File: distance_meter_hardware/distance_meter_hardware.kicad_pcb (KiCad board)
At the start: 2 copper layers, 95.5 x 55.5 mm, 6 parts, among them J1 PPPC071LFBN-RC, J2 PPPC071LFBN-RC, J3 PPPC141LFBN-RC, J4 PPPC141LFBN-RC, J5 PPPC071LFBN-RC, J6 PPPC071LFBN-RC

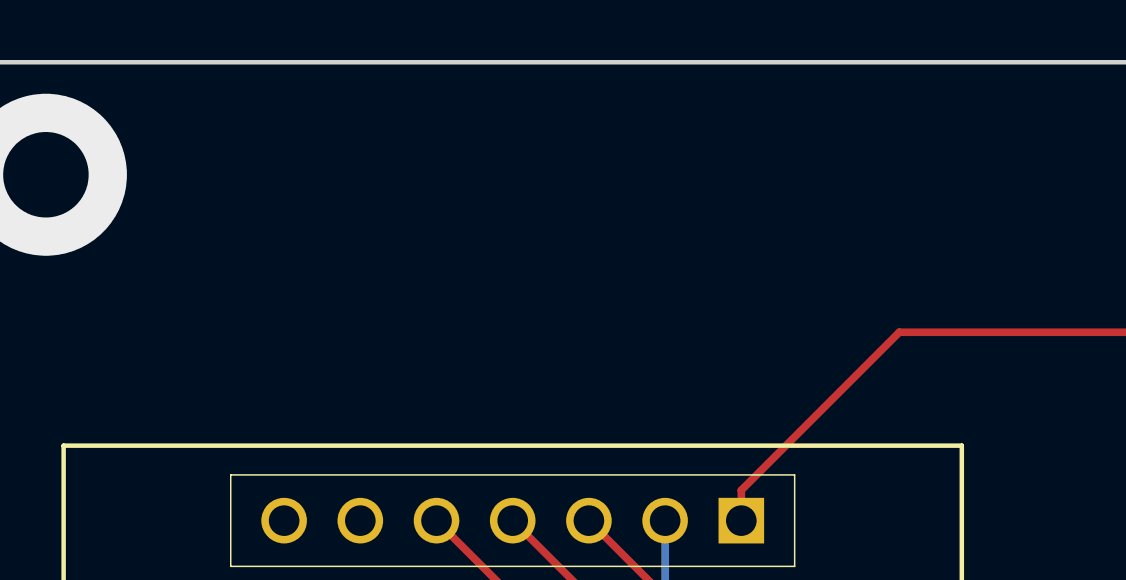
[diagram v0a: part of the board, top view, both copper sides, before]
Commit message: Add logo to PCB layout. Move measures to user-defined layer
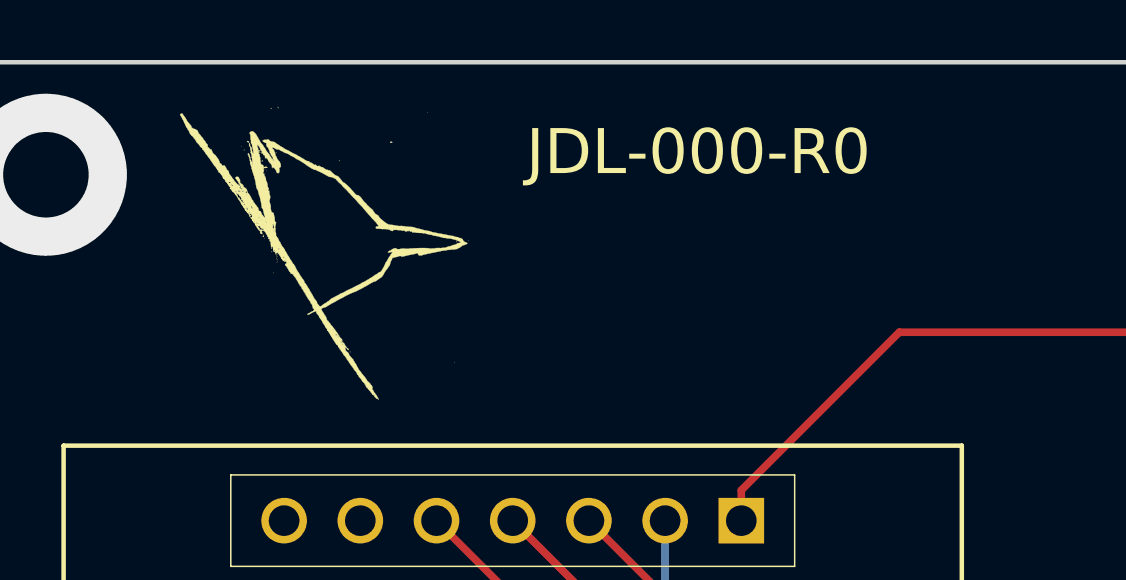
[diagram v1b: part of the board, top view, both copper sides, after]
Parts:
- added G***: LOGO, pictures:jaybird-logo-small, F.Cu at (71.4, 47.5)
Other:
- board text added: "JDL-000-R0"

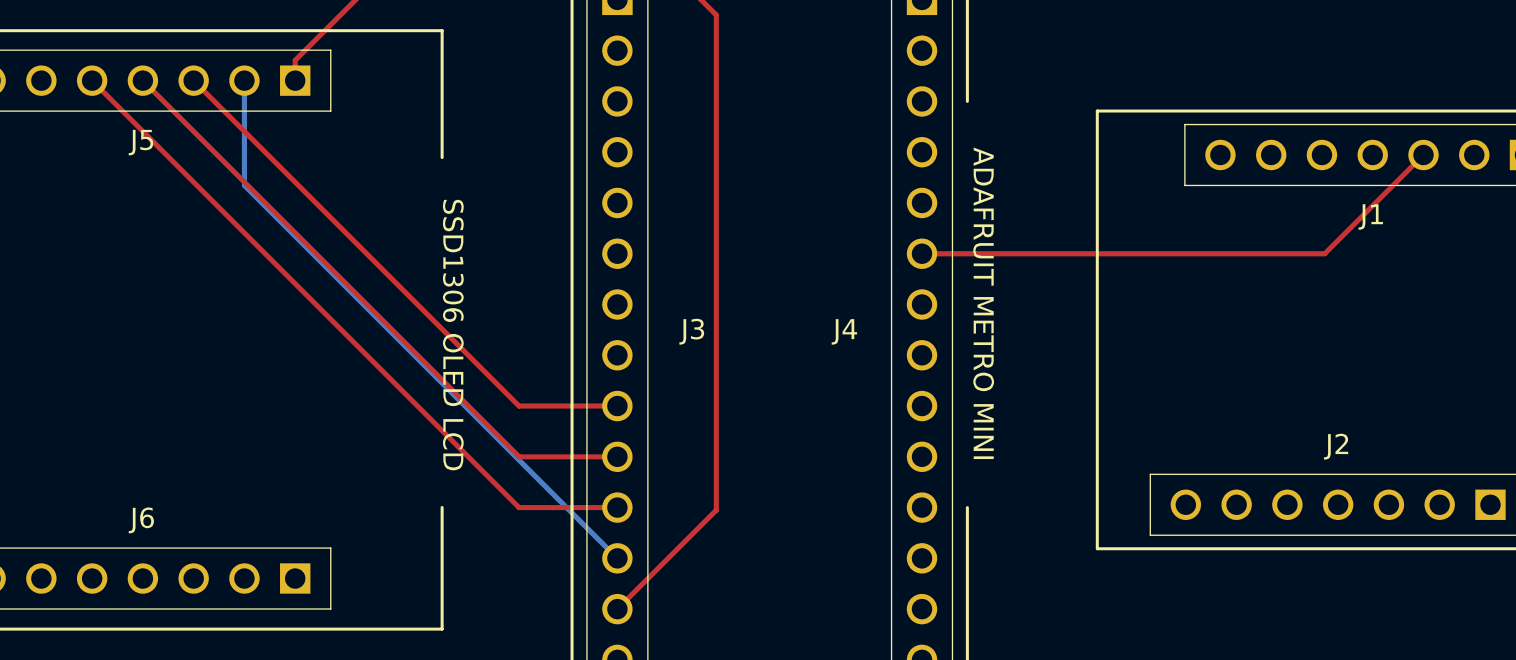
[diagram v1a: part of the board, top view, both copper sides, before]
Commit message: Add project information to schematic sheet. Re-annotate schematic.
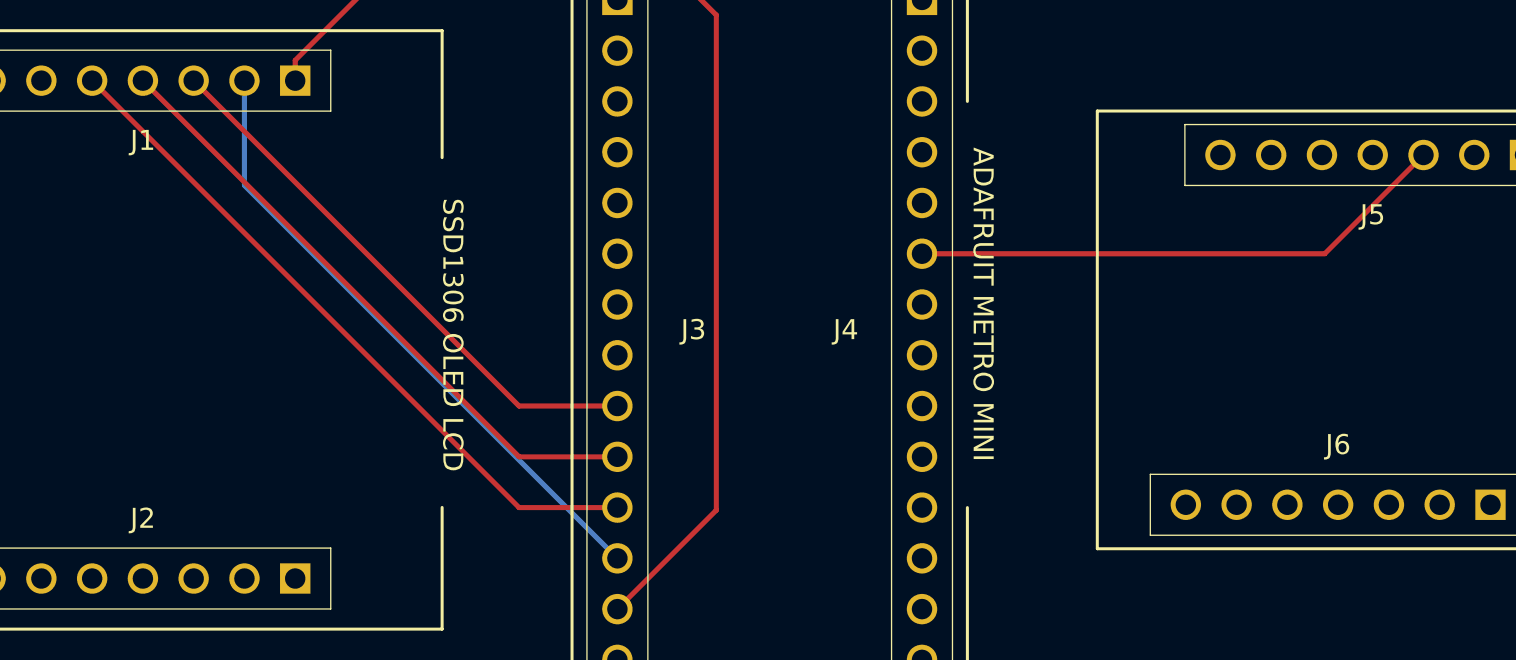
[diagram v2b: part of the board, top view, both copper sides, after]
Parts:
- renumbered J5 to J1, J6 to J2, J1 to J5, J2 to J6
